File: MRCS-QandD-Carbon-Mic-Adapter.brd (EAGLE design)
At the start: 49.8 x 68.8 mm, 12 parts, among them CON1 DC PWR, CON2 Output

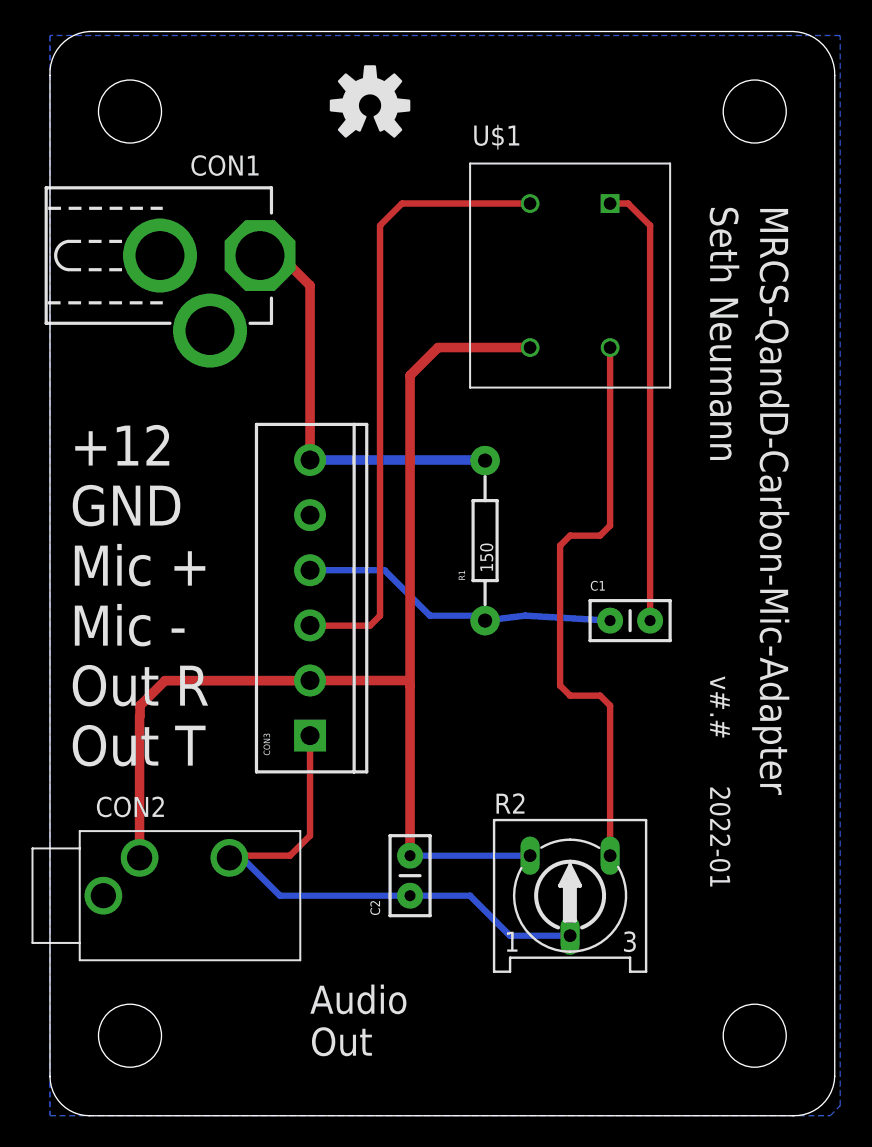
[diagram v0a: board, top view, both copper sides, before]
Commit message: Version 1.1 fixed input ground, general cleanup
Version 1.1 fixed input ground, general cleanup
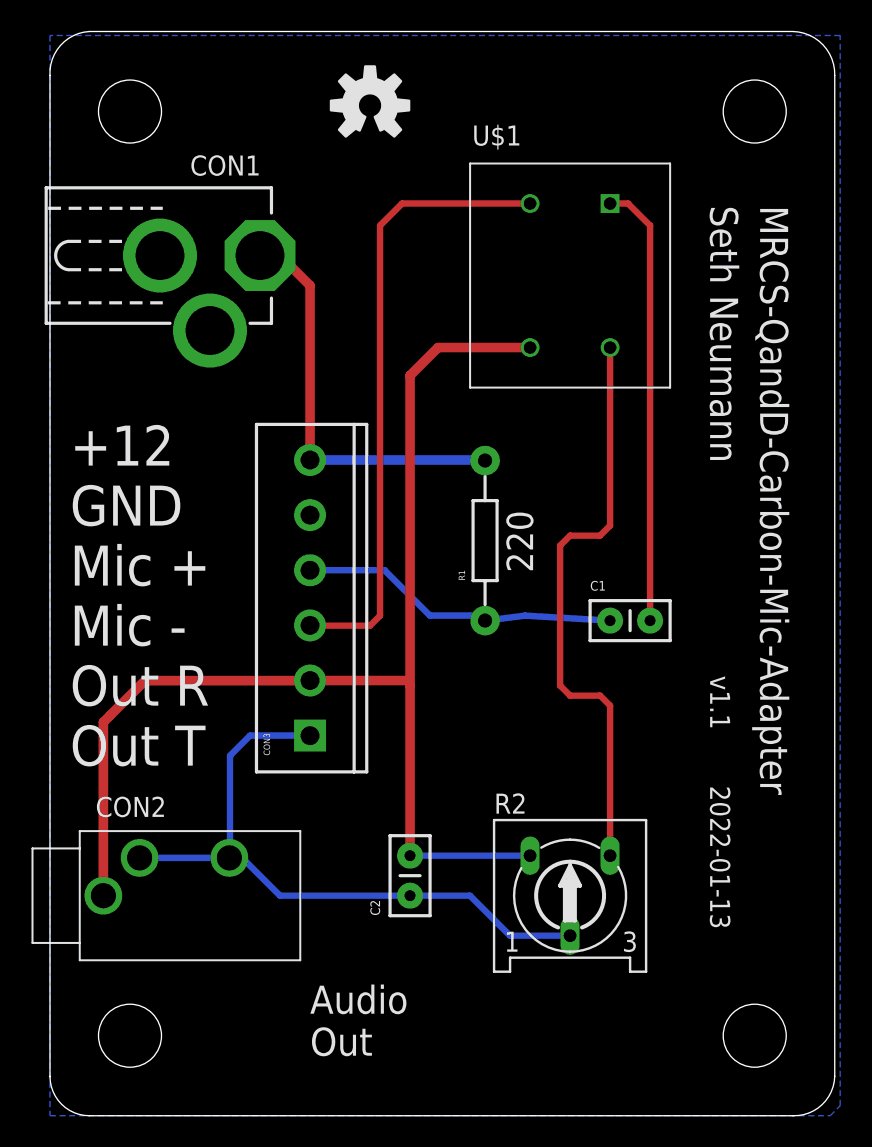
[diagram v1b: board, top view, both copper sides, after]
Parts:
- R1: value 150 -> 220
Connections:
- removed net OUTR: CON3.3, U$1.PBOTTOM
- net GND: now also CON3.3, U$1.PBOTTOM; no longer CON2.GND
- net N$7: now also CON2.TIP
- net OUTT: now also CON2.GND; no longer CON2.TIP
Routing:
- net OUTR: track 39.6 -> 0.00 mm
- net GND: track 0.00 -> 39.6 mm
- net N$7: track 35.7 -> 41.5 mm
- net OUTT: track 74.1 -> 78.2 mm
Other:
- board text added: "2022-01-13"
- board text added: "v1.1"
- board text removed: "2022-01"
- board text removed: "v#.#"
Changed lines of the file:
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@@
 <setting verticaltext="up"/>
 </settings>
-<grid distance="25" unitdist="mil" unit="mil" style="dots" multiple="2" display="yes" altdistance="12.5" altunitdist="mil" altunit="mil"/>
+<grid distance="50" unitdist="mil" unit="mil" style="dots" multiple="2" display="yes" altdistance="25" altunitdist="mil" altunit="mil"/>
 <layers>
 <layer number="1" name="Top" color="4" fill="1" visible="yes" active="yes"/>
@@
 <plain>
 <text x="45.085" y="57.785" size="1.778" layer="21" font="vector" ratio="10" rot="SR270">&gt;DRAWING_NAME </text>
-<text x="41.91" y="20.955" size="1.27" layer="21" font="vector" ratio="10" rot="SR270">2022-01</text>
-<text x="41.91" y="27.94" size="1.27" layer="21" font="vector" ratio="10" rot="SR270">v#.#</text>
+<text x="41.91" y="20.955" size="1.27" layer="21" font="vector" ratio="10" rot="SR270">2022-01-13</text>
+<text x="41.91" y="27.94" size="1.27" layer="21" font="vector" ratio="10" rot="SR270">v1.1</text>
 <text x="7.62" y="105.41" size="1.016" layer="48" font="vector" ratio="10">Use tPlace/bPlace for silkscreen text and drawings
 Use Document, tDocu and bDocu for assembly notes and documentation that does NOT go on the board</text>
@@
 <element name="OSHW1" library="SPCoast" package="OSHW-LOGO-M" value="DOC-OSHW-LOGO-M" x="20.32" y="64.135"/>
 <element name="C1" library="SPCoast" package="C-PTH-0.100" value="1.0 uF" x="36.83" y="31.4325"/>
-<element name="R1" library="SPCoast" package="AXIAL-0.4-RES" value="150" x="27.6225" y="36.5125" rot="R90"/>
+<element name="R1" library="SPCoast" package="AXIAL-0.4-RES" value="220" x="27.6225" y="36.5125" smashed="yes" rot="R90">
+<attribute name="NAME" x="26.3525" y="33.9725" size="0.4064" layer="25" rot="R90"/>
+<attribute name="VALUE" x="30.6705" y="34.4805" size="1.6764" layer="21" ratio="15" rot="R90"/>
+</element>
 <element name="CON2" library="SPCoast" package="AUDIO-JACK-3.5MM_STEREO" value="Output" x="8.89" y="13.97"/>
 <element name="U$1" library="MRCS" package="XFMR580X500" value="EI14_600-600" x="33.02" y="53.34"/>
 <element name="CON3" library="SPCoast" package="SCREWTERMINAL-3.5MM-6" value="" x="16.51" y="24.13" rot="R90"/>
-<element name="CON1" library="SPCoast" package="DCJ0202" value="DC PWR" x="10.16" y="54.61" rot="R270"/>
+<element name="CON1" library="SPCoast" package="DCJ0202" value="DC PWR" x="10.16" y="54.61" smashed="yes" rot="R270">
+<attribute name="NAME" x="8.89" y="59.69" size="1.27" layer="25"/>
+<attribute name="VALUE" x="8.89" y="62.23" size="1.27" layer="27"/>
+</element>
 <element name="R2" library="pot" package="RS3" value="1K" x="33.02" y="13.97"/>
 <element name="U$2" library="SPCoast" package="BOARD-DINRAIL-2.7IN-5CM" value="" x="0" y="0"/>
@@
 <signal name="GND">
 <contactref element="CON1" pad="3"/>
-<contactref element="CON2" pad="GND"/>
 <contactref element="CON1" pad="2"/>
 <contactref element="CON3" pad="5"/>
@@
 <vertex x="0" y="68.58"/>
 </polygon>
+<contactref element="CON3" pad="3"/>
+<contactref element="U$1" pad="PBOTTOM"/>
+<wire x1="30.48" y1="57.912" x2="22.352" y2="57.912" width="0.4064" layer="1"/>
+<wire x1="22.352" y1="57.912" x2="20.955" y2="56.515" width="0.4064" layer="1"/>
+<wire x1="20.955" y1="56.515" x2="20.955" y2="31.75" width="0.4064" layer="1"/>
+<wire x1="20.955" y1="31.75" x2="20.32" y2="31.115" width="0.4064" layer="1"/>
+<wire x1="20.32" y1="31.115" x2="16.525" y2="31.115" width="0.4064" layer="1"/>
+<wire x1="16.525" y1="31.115" x2="16.51" y2="31.13" width="0.4064" layer="1"/>
 </signal>
 <signal name="MIC+">
@@
 <wire x1="36.703" y1="57.912" x2="38.1" y2="56.515" width="0.4064" layer="1"/>
 <wire x1="38.1" y1="56.515" x2="38.1" y2="31.4325" width="0.4064" layer="1"/>
-</signal>
-<signal name="OUTR">
-<contactref element="CON3" pad="3"/>
-<contactref element="U$1" pad="PBOTTOM"/>
-<wire x1="30.48" y1="57.912" x2="22.352" y2="57.912" width="0.4064" layer="1"/>
-<wire x1="22.352" y1="57.912" x2="20.955" y2="56.515" width="0.4064" layer="1"/>
-<wire x1="20.955" y1="56.515" x2="20.955" y2="31.75" width="0.4064" layer="1"/>
-<wire x1="20.955" y1="31.75" x2="20.32" y2="31.115" width="0.4064" layer="1"/>
-<wire x1="20.32" y1="31.115" x2="16.525" y2="31.115" width="0.4064" layer="1"/>
-<wire x1="16.525" y1="31.115" x2="16.51" y2="31.13" width="0.4064" layer="1"/>
 </signal>
 <signal name="N$1">
@@
 <contactref element="U$1" pad="SBOTTOM"/>
 <contactref element="R2" pad="A"/>
-<contactref element="CON2" pad="TIP"/>
 <contactref element="CON3" pad="2"/>
 <contactref element="C2" pad="2"/>
@@
 <wire x1="22.86" y1="46.99" x2="22.86" y2="27.305" width="0.6096" layer="1"/>
 <wire x1="22.86" y1="27.305" x2="22.86" y2="16.51" width="0.6096" layer="1"/>
-<wire x1="5.69" y1="16.37" x2="5.69" y2="25.375" width="0.6096" layer="1"/>
-<wire x1="5.69" y1="25.375" x2="5.715" y2="25.4" width="0.4064" layer="1"/>
-<wire x1="5.715" y1="25.4" x2="5.715" y2="26.035" width="0.6096" layer="1"/>
-<wire x1="5.715" y1="26.035" x2="7.3025" y2="27.6225" width="0.6096" layer="1"/>
-<wire x1="7.3025" y1="27.6225" x2="16.5025" y2="27.6225" width="0.6096" layer="1"/>
+<wire x1="6.0325" y1="27.6225" x2="16.5025" y2="27.6225" width="0.6096" layer="1"/>
 <wire x1="16.5025" y1="27.6225" x2="16.51" y2="27.63" width="0.4064" layer="1"/>
 <wire x1="16.51" y1="27.63" x2="22.535" y2="27.63" width="0.6096" layer="1"/>
 <wire x1="22.535" y1="27.63" x2="22.86" y2="27.305" width="0.4064" layer="1"/>
 <wire x1="22.86" y1="16.51" x2="30.48" y2="16.51" width="0.4064" layer="16"/>
+<contactref element="CON2" pad="GND"/>
+<wire x1="3.39" y1="13.97" x2="3.39" y2="24.98" width="0.6096" layer="1"/>
+<wire x1="3.39" y1="24.98" x2="3.81" y2="25.4" width="0.6096" layer="1"/>
+<wire x1="6.0325" y1="27.6225" x2="3.81" y2="25.4" width="0.6096" layer="1"/>
 </signal>
 <signal name="N$7">
-<contactref element="CON2" pad="RING"/>
 <contactref element="R2" pad="S"/>
-<contactref element="CON3" pad="1"/>
 <contactref element="C2" pad="1"/>
 <wire x1="22.86" y1="13.97" x2="26.67" y2="13.97" width="0.4064" layer="16"/>
 <wire x1="26.67" y1="13.97" x2="29.21" y2="11.43" width="0.4064" layer="16"/>
 <wire x1="29.21" y1="11.43" x2="33.02" y2="11.43" width="0.4064" layer="16"/>
-<wire x1="11.39" y1="16.37" x2="12.205" y2="16.37" width="0.4064" layer="16"/>
 <wire x1="12.205" y1="16.37" x2="14.605" y2="13.97" width="0.4064" layer="16"/>
 <wire x1="14.605" y1="13.97" x2="22.86" y2="13.97" width="0.4064" layer="16"/>
-<wire x1="16.51" y1="24.13" x2="16.51" y2="17.78" width="0.4064" layer="1"/>
-<wire x1="16.51" y1="17.78" x2="15.24" y2="16.51" width="0.4064" layer="1"/>
-<wire x1="15.24" y1="16.51" x2="11.53" y2="16.51" width="0.4064" layer="1"/>
-<wire x1="11.53" y1="16.51" x2="11.39" y2="16.37" width="0.4064" layer="1"/>
+<contactref element="CON2" pad="TIP"/>
+<contactref element="CON2" pad="RING"/>
+<contactref element="CON3" pad="1"/>
+<wire x1="5.69" y1="16.37" x2="11.39" y2="16.37" width="0.4064" layer="16"/>
+<wire x1="16.51" y1="24.13" x2="12.7" y2="24.13" width="0.4064" layer="16"/>
+<wire x1="12.7" y1="24.13" x2="11.43" y2="22.86" width="0.4064" layer="16"/>
+<wire x1="11.43" y1="22.86" x2="11.43" y2="16.41" width="0.4064" layer="16"/>
+<wire x1="11.43" y1="16.41" x2="11.39" y2="16.37" width="0.4064" layer="16"/>
+<wire x1="12.205" y1="16.37" x2="11.39" y2="16.37" width="0.4064" layer="16"/>
 </signal>
 </signals>
